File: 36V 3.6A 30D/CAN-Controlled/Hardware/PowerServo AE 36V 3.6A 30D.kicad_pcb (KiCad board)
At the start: 4 copper layers, 35.7 x 35.5 mm, 36 parts, among them IC1 DRV8251DDAR, J1 Control_In, J2 MOT_A, J3 Prog_IN, J4 Power_In, J5 Power_In, J6 Control_In, J7 MOT_B, U1 LMZM23601V5, U2 TLV76733DRVx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

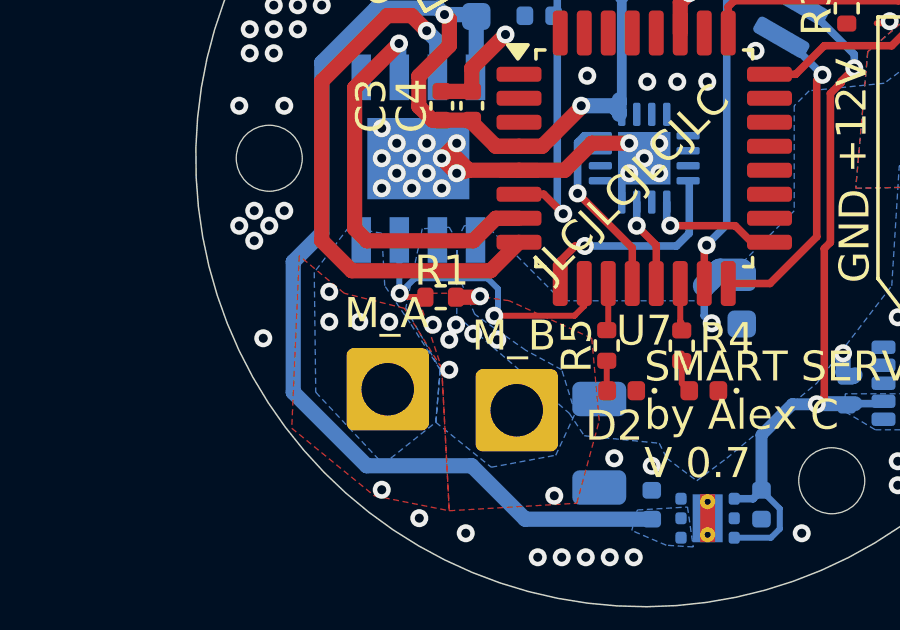
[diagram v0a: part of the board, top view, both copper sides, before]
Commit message: Fixed driver error
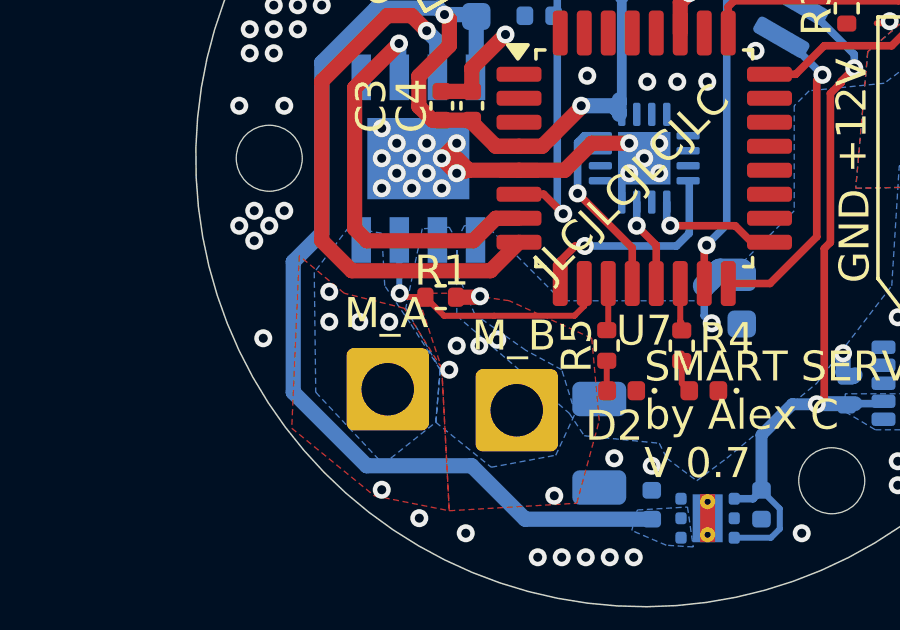
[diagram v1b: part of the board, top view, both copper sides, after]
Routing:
- net ISEN: track 11.2 -> 9.13 mm, vias 2 -> 1
- net Net-(IC1-OUT1): vias 6 -> 4
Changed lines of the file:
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@@
+	)
+	(segment
+		(start 86.205 77.381751)
+		(end 86.824998 78.001749)
+		(width 0.2)
+		(layer "F.Cu")
+		(net 6)
+	)
+	(segment
+		(start 86.824998 78.001749)
+		(end 88.498251 78.001749)
+		(width 0.2)
+		(layer "F.Cu")
+		(net 6)
+	)
+	(segment
+		(start 88.498251 78.001749)
+		(end 88.5 78)
+		(width 0.2)
+		(layer "F.Cu")
+		(net 6)
 	)
 	(segment
@@
 	)
 	(via
-		(at 88.5 78)
-		(size 0.6)
-		(drill 0.3)
-		(layers "F.Cu" "B.Cu")
-		(net 6)
-	)
-	(via
 		(at 85.35 77.254)
 		(size 0.6)
@@
 	)
 	(segment
-		(start 88.5 78)
-		(end 88.625 77.875)
-		(width 0.2)
-		(layer "B.Cu")
-		(net 6)
-	)
-	(segment
 		(start 85.334999 75.474999)
 		(end 85.334999 77.238999)
-		(width 0.2)
-		(layer "B.Cu")
-		(net 6)
-	)
-	(segment
-		(start 85.854 76.75)
-		(end 85.35 77.254)
-		(width 0.2)
-		(layer "B.Cu")
-		(net 6)
-	)
-	(segment
-		(start 88.273529 76.75)
-		(end 85.854 76.75)
-		(width 0.2)
-		(layer "B.Cu")
-		(net 6)
-	)
-	(segment
-		(start 88.625 77.875)
-		(end 88.625 77.101471)
-		(width 0.2)
-		(layer "B.Cu")
-		(net 6)
-	)
-	(segment
-		(start 88.625 77.101471)
-		(end 88.273529 76.75)
 		(width 0.2)
 		(layer "B.Cu")
@@
 	)
 	(via
-		(at 86.45 78.3)
+		(at 87.25 79)
 		(size 0.6)
 		(drill 0.3)
@@
 	)
 	(via
-		(at 87.8 78.6)
+		(at 88 79)
 		(size 0.6)
 		(drill 0.3)
-		(layers "F.Cu" "B.Cu")
-		(free yes)
-		(net 8)
-	)
-	(via
-		(at 87 78.8)
-		(size 0.6)
-		(drill 0.3)
-		(layers "F.Cu" "B.Cu")
-		(free yes)
-		(net 8)
-	)
-	(via
-		(at 87.225 78.3)
-		(size 0.6)
-		(drill 0.3)
